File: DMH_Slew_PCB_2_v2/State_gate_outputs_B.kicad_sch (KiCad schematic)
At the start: 26 parts, among them J10 TS_Jack_6.35mm_Sw, J61 Conn_01x08_PinHeader, J9 TS_Jack_6.35mm_Sw, Q11 BC548, Q12 BC548, U3 TL074

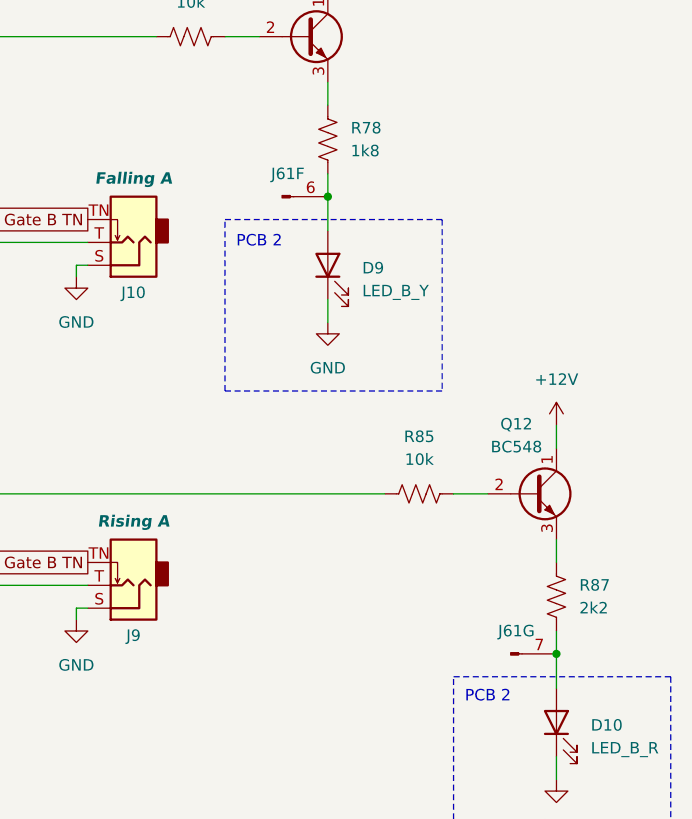
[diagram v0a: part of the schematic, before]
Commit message: PCB 2 component placement done
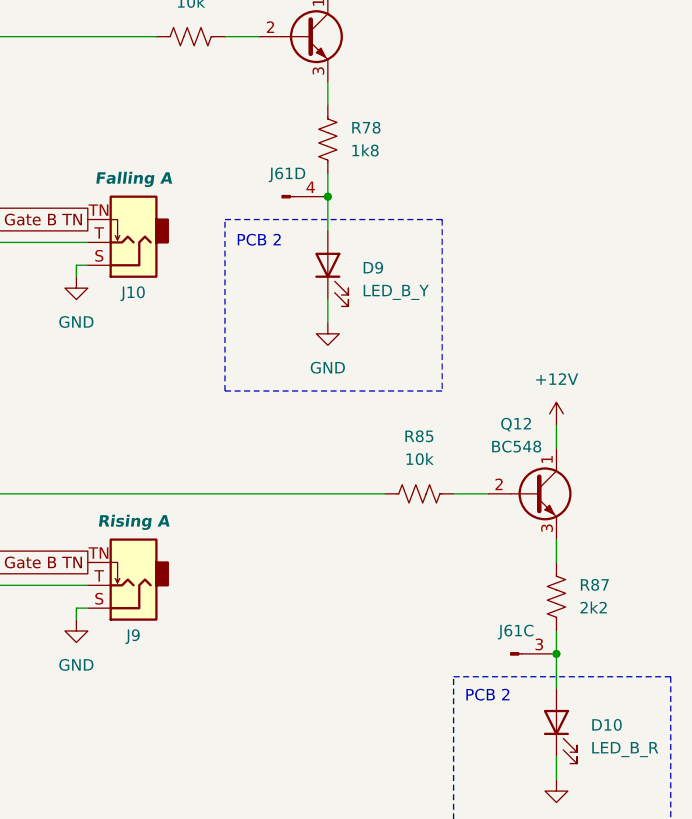
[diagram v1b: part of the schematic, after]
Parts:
- J61: footprint Connector_PinHeader_2.54mm:PinHeader_1x08_P2.54mm_Vertical -> Connector_PinSocket_2.54mm:PinSocket_1x08_P2.54mm_Vertical
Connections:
- net at D10.2 (A), R87.2: now also J61.3 (Pin_3); no longer J61.7 (Pin_7)
- net at D9.2 (A), R78.2: now also J61.4 (Pin_4); no longer J61.6 (Pin_6)
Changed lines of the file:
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@@
 		(lib_id "SynthStuff:Conn_01x08_PinHeader")
 		(at 251.46 106.68 0)
-		(unit 7)
+		(unit 3)
 		(exclude_from_sim no)
 		(in_bom yes)
@@
 			)
 		)
-		(property "Footprint" "Connector_PinHeader_2.54mm:PinHeader_1x08_P2.54mm_Vertical"
+		(property "Footprint" "Connector_PinSocket_2.54mm:PinSocket_1x08_P2.54mm_Vertical"
 			(at 251.46 106.68 0)
 			(effects
@@
 			)
 		)
+		(property "Function" ""
+			(at 251.46 106.68 0)
+			(effects
+				(font
+					(size 1.27 1.27)
+				)
+			)
+		)
 		(pin "3"
 		)
@@
 				(path "/58f4306d-5387-4983-bb08-41a2313fd315/a1b8698d-b4e4-404a-8e9c-ccbb5494e3d6"
 					(reference "J61")
-					(unit 7)
+					(unit 3)
 				)
 			)
@@
 		(lib_id "SynthStuff:Conn_01x08_PinHeader")
 		(at 226.06 55.88 0)
-		(unit 6)
+		(unit 4)
 		(exclude_from_sim no)
 		(in_bom yes)
@@
 			)
 		)
-		(property "Footprint" "Connector_PinHeader_2.54mm:PinHeader_1x08_P2.54mm_Vertical"
+		(property "Footprint" "Connector_PinSocket_2.54mm:PinSocket_1x08_P2.54mm_Vertical"
 			(at 226.06 55.88 0)
 			(effects
@@
 			)
 		)
+		(property "Function" ""
+			(at 226.06 55.88 0)
+			(effects
+				(font
+					(size 1.27 1.27)
+				)
+			)
+		)
 		(pin "3"
 		)
@@
 				(path "/58f4306d-5387-4983-bb08-41a2313fd315/a1b8698d-b4e4-404a-8e9c-ccbb5494e3d6"
 					(reference "J61")
-					(unit 6)
-				)
-			)
+					(unit 4)
+				)
+			)

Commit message: PCB 1 component placement ongoing
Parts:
- J10: Function Falling A -> Falling B
- J9: Function Rising A -> Rising B
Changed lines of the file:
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@@
 			)
 		)
-		(property "Function" "Falling A"
+		(property "Function" "Falling B"
 			(at 209.55 53.848 0)
 			(effects
@@
 			)
 		)
-		(property "Function" "Rising A"
+		(property "Function" "Rising B"
 			(at 209.55 91.948 0)
 			(effects
